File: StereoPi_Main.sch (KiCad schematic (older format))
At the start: 39 parts

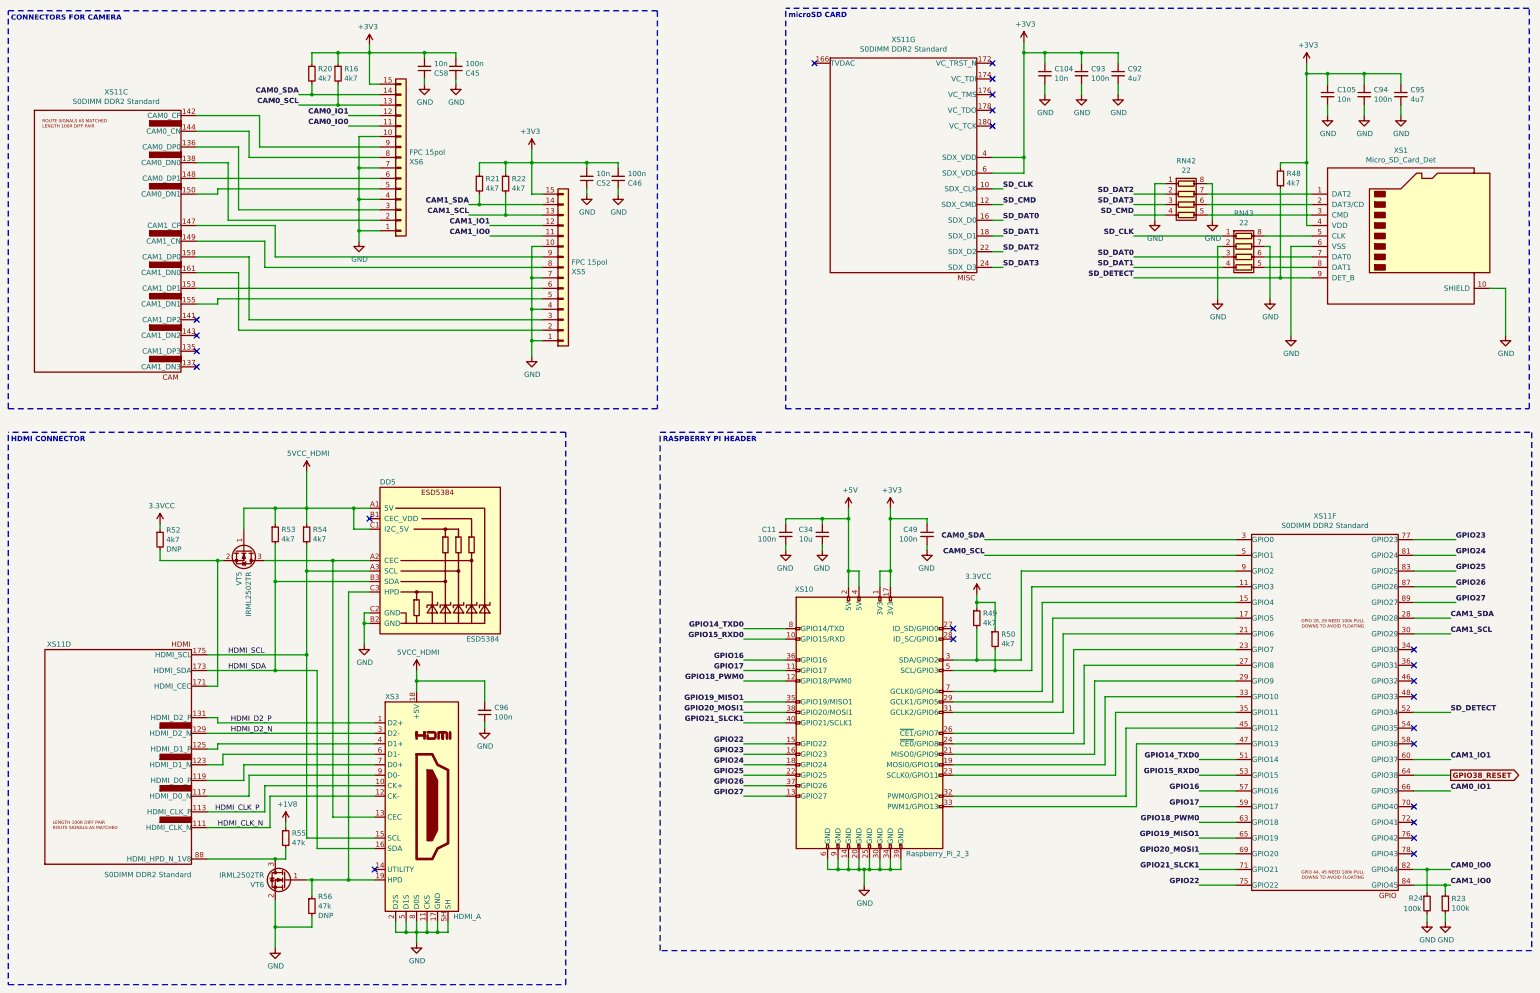
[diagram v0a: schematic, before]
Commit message: added Voltages to Caps, reformatted labels
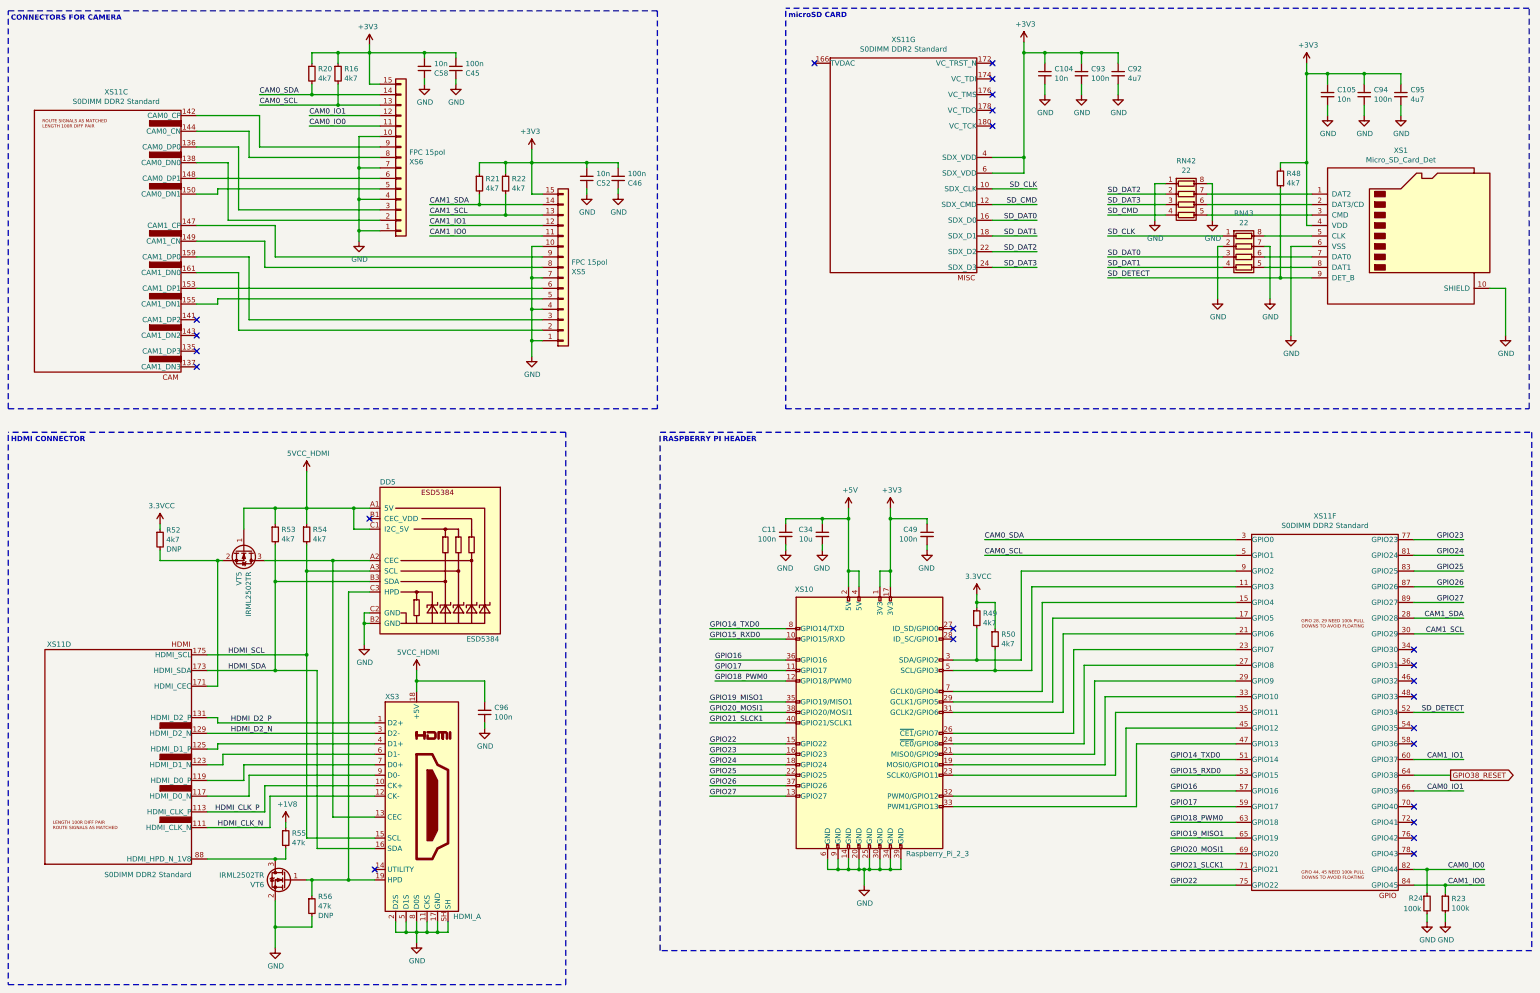
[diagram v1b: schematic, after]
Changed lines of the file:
@@
 EESchema Schematic File Version 4
 LIBS:StereoPi-cache
-EELAYER 26 0
+EELAYER 30 0
 EELAYER END
 $Descr A3 16535 11693
@@
 Wire Wire Line
 	2850 2300 4600 2300
-Text Label 14825 8900 0    50   ~ 10
+Text Label 15150 8900 2    50   ~ 0
 CAM0_IO0
 Wire Wire Line
-	14825 8900 14600 8900
-Text Label 14825 8150 0    50   ~ 10
+	15150 8900 14600 8900
+Text Label 14950 8150 2    50   ~ 0
 CAM0_IO1
-Text Label 10375 5900 2    50   ~ 10
+Text Label 10375 5900 0    50   ~ 0
 CAM0_SCL
-Text Label 10375 5750 2    50   ~ 10
+Text Label 10375 5750 0    50   ~ 0
 CAM0_SDA
 Wire Wire Line
-	14825 8150 14475 8150
-Text Label 3825 1500 2    50   ~ 10
+	14950 8150 14475 8150
+Text Label 3450 1500 0    50   ~ 0
 CAM0_SDA
-Text Label 3825 1600 2    50   ~ 10
+Text Label 3450 1600 0    50   ~ 0
 CAM0_SCL
-Text Label 4300 1800 2    50   ~ 10
+Text Label 3925 1800 0    50   ~ 0
 CAM0_IO0
-Text Label 4300 1700 2    50   ~ 10
+Text Label 3925 1700 0    50   ~ 0
 CAM0_IO1
 Wire Wire Line
-	4600 1700 4300 1700
-Wire Wire Line
-	4600 1800 4300 1800
+	4600 1700 3925 1700
+Wire Wire Line
+	4600 1800 3925 1800
 $Comp
 L power:GND #PWR0108
@@
 Wire Wire Line
 	4400 2200 4400 2500
-Text Label 14825 9050 0    50   ~ 10
+Text Label 15150 9050 2    50   ~ 0
 CAM1_IO0
 Wire Wire Line
-	14825 9050 14775 9050
-Text Label 5650 2850 2    50   ~ 10
+	15150 9050 14775 9050
+Text Label 5075 2850 0    50   ~ 0
 CAM1_IO0
-Text Label 14825 7850 0    50   ~ 10
+Text Label 14950 7850 2    50   ~ 0
 CAM1_IO1
 Wire Wire Line
-	14825 7850 14475 7850
-Text Label 5650 2750 2    50   ~ 10
+	14950 7850 14475 7850
+Text Label 5075 2750 0    50   ~ 0
 CAM1_IO1
-Text Label 14825 6650 0    50   ~ 10
+Text Label 14950 6650 2    50   ~ 0
 CAM1_SCL
-Text Label 14825 6500 0    50   ~ 10
+Text Label 14950 6500 2    50   ~ 0
 CAM1_SDA
-Text Label 5450 2650 2    50   ~ 10
+Text Label 5075 2650 0    50   ~ 0
 CAM1_SCL
-Text Label 5450 2550 2    50   ~ 10
+Text Label 5075 2550 0    50   ~ 0
 CAM1_SDA
 Wire Wire Line
-	14825 6500 14475 6500
-Wire Wire Line
-	14825 6650 14475 6650
-Wire Wire Line
-	5450 2550 5550 2550
-Wire Wire Line
-	5450 2650 5800 2650
-Wire Wire Line
-	5650 2750 6150 2750
-Wire Wire Line
-	5650 2850 6150 2850
+	14950 6500 14475 6500
+Wire Wire Line
+	14950 6650 14475 6650
+Wire Wire Line
+	5075 2550 5550 2550
+Wire Wire Line
+	5075 2650 5800 2650
+Wire Wire Line
+	5075 2750 6150 2750
+Wire Wire Line
+	5075 2850 6150 2850
 $Comp
 L Connector:Raspberry_Pi_2_3 XS10
@@
 	1    0    0    -1
 $EndComp
-Text Label 14825 7400 0    50   ~ 10
+Text Label 14950 7400 2    50   ~ 0
 SD_DETECT
 Wire Wire Line
-	14475 7400 14825 7400
-Text Label 11800 3250 2    50   ~ 10
+	14475 7400 14950 7400
+Text Label 11550 3250 0    50   ~ 0
 SD_DETECT
 Wire Wire Line
-	11800 3250 13200 3250
+	11550 3250 13200 3250
 $Comp
 L Device:R_Small R48
@@
 NoConn ~ 10450 1800
 NoConn ~ 8750 1200
-Text Label 11800 2450 2    50   ~ 10
+Text Label 11550 2450 0    50   ~ 0
 SD_DAT2
-Text Label 11800 2550 2    50   ~ 10
+Text Label 11550 2550 0    50   ~ 0
 SD_DAT3
-Text Label 11800 3050 2    50   ~ 10
+Text Label 11550 3050 0    50   ~ 0
 SD_DAT0
-Text Label 11800 3150 2    50   ~ 10
+Text Label 11550 3150 0    50   ~ 0
 SD_DAT1
-Text Label 10550 3000 0    50   ~ 10
+Text Label 10875 3000 2    50   ~ 0
 SD_DAT2
-Text Label 10550 3150 0    50   ~ 10
+Text Label 10875 3150 2    50   ~ 0
 SD_DAT3
-Text Label 10550 2700 0    50   ~ 10
+Text Label 10875 2700 2    50   ~ 0
 SD_DAT0
-Text Label 10550 2850 0    50   ~ 10
+Text Label 10875 2850 2    50   ~ 0
 SD_DAT1
 Wire Wire Line
-	10550 2700 10450 2700
-Wire Wire Line
-	10550 2850 10450 2850
-Wire Wire Line
-	10550 3000 10450 3000
-Wire Wire Line
-	10550 3150 10450 3150
-Text Label 11800 2650 2    50   ~ 10
+	10875 2700 10450 2700
+Wire Wire Line
+	10875 2850 10450 2850
+Wire Wire Line
+	10875 3000 10450 3000
+Wire Wire Line
+	10875 3150 10450 3150
+Text Label 11550 2650 0    50   ~ 0
 SD_CMD
-Text Label 11800 2850 2    50   ~ 10
+Text Label 11550 2850 0    50   ~ 0
 SD_CLK
 Wire Wire Line
 	13500 2850 13050 2850
-Text Label 10550 2400 0    50   ~ 10
+Text Label 10875 2400 2    50   ~ 0
 SD_CLK
-Text Label 10550 2550 0    50   ~ 10
+Text Label 10875 2550 2    50   ~ 0
 SD_CMD
 Wire Wire Line
-	10550 2400 10450 2400
-Wire Wire Line
-	10550 2550 10450 2550
+	10875 2400 10450 2400
+Wire Wire Line
+	10875 2550 10450 2550
 $Comp
 L Device:R_Pack04 RN42
@@
 	13500 2650 12500 2650
 Wire Wire Line
-	12100 2450 11800 2450
-Wire Wire Line
-	12100 2550 11800 2550
-Wire Wire Line
-	12100 2650 11800 2650
+	12100 2450 11550 2450
+Wire Wire Line
+	12100 2550 11550 2550
+Wire Wire Line
+	12100 2650 11550 2650
 $Comp
 L Device:R_Pack04 RN43
@@
 	13500 3150 13050 3150
 Wire Wire Line
-	12650 2850 11800 2850
-Wire Wire Line
-	12650 3050 11800 3050
-Wire Wire Line
-	12650 3150 11800 3150
+	12650 2850 11550 2850
+Wire Wire Line
+	12650 3050 11550 3050
+Wire Wire Line
+	12650 3150 11550 3150
 $Comp
 L power:GND #PWR0126
@@
 Wire Wire Line
 	11825 7700 12775 7700
-Text Label 12425 7850 2    50   ~ 10
+Text Label 12150 7850 0    50   ~ 0
 GPIO14_TXD0
-Text Label 12425 8000 2    50   ~ 10
+Text Label 12150 8000 0    50   ~ 0
 GPIO15_RXD0
-Text Label 12425 8150 2    50   ~ 10
+Text Label 12150 8150 0    50   ~ 0
 GPIO16
-Text Label 12425 8300 2    50   ~ 10
+Text Label 12150 8300 0    50   ~ 0
 GPIO17
-Text Label 12425 8450 2    50   ~ 10
+Text Label 12150 8450 0    50   ~ 0
 GPIO18_PWM0
-Text Label 12425 8600 2    50   ~ 10
+Text Label 12150 8600 0    50   ~ 0
 GPIO19_MISO1
-Text Label 12425 8750 2    50   ~ 10
+Text Label 12150 8750 0    50   ~ 0
 GPIO20_MOSI1
-Text Label 12425 8900 2    50   ~ 10
+Text Label 12150 8900 0    50   ~ 0
 GPIO21_SLCK1
-Text Label 12425 9050 2    50   ~ 10
+Text Label 12150 9050 0    50   ~ 0
 GPIO22
-Text Label 8075 6600 2    50   ~ 10
+Text Label 7750 6600 0    50   ~ 0
 GPIO14_TXD0
-Text Label 8075 6700 2    50   ~ 10
+Text Label 7750 6700 0    50   ~ 0
 GPIO15_RXD0
-Text Label 8075 6900 2    50   ~ 10
+Text Label 7800 6900 0    50   ~ 0
 GPIO16
-Text Label 8075 7000 2    50   ~ 10
+Text Label 7800 7000 0    50   ~ 0
 GPIO17
-Text Label 8075 7100 2    50   ~ 10
+Text Label 7800 7100 0    50   ~ 0
 GPIO18_PWM0
-Text Label 8075 7300 2    50   ~ 10
+Text Label 7750 7300 0    50   ~ 0
 GPIO19_MISO1
-Text Label 8075 7400 2    50   ~ 10
+Text Label 7750 7400 0    50   ~ 0
 GPIO20_MOSI1
-Text Label 8075 7500 2    50   ~ 10
+Text Label 7750 7500 0    50   ~ 0
 GPIO21_SLCK1
-Text Label 8075 7700 2    50   ~ 10
+Text Label 7750 7700 0    50   ~ 0
 GPIO22
-Text Label 14875 5750 0    50   ~ 10
+Text Label 14950 5750 2    50   ~ 0
 GPIO23
-Text Label 14875 5900 0    50   ~ 10
+Text Label 14950 5900 2    50   ~ 0
 GPIO24
-Text Label 14875 6050 0    50   ~ 10
+Text Label 14950 6050 2    50   ~ 0
 GPIO25
-Text Label 14875 6200 0    50   ~ 10
+Text Label 14950 6200 2    50   ~ 0
 GPIO26
-Text Label 14875 6350 0    50   ~ 10
+Text Label 14950 6350 2    50   ~ 0
 GPIO27
 Wire Wire Line
-	14875 6350 14475 6350
-Wire Wire Line
-	14875 6200 14475 6200
-Wire Wire Line
-	14875 6050 14475 6050
-Wire Wire Line
-	14875 5900 14475 5900
-Wire Wire Line
-	14875 5750 14475 5750
-Text Label 8075 7800 2    50   ~ 10
+	14950 6350 14475 6350
+Wire Wire Line
+	14950 6200 14475 6200
+Wire Wire Line
+	14950 6050 14475 6050
+Wire Wire Line
+	14950 5900 14475 5900
+Wire Wire Line
+	14950 5750 14475 5750
+Text Label 7750 7800 0    50   ~ 0
 GPIO23
-Text Label 8075 7900 2    50   ~ 10
+Text Label 7750 7900 0    50   ~ 0
 GPIO24
-Text Label 8075 8000 2    50   ~ 10
+Text Label 7750 8000 0    50   ~ 0
 GPIO25
-Text Label 8075 8100 2    50   ~ 10
+Text Label 7750 8100 0    50   ~ 0
 GPIO26
-Text Label 8075 8200 2    50   ~ 10
+Text Label 7750 8200 0    50   ~ 0
 GPIO27
 Wire Wire Line
-	8075 7700 8475 7700
-Wire Wire Line
-	8075 7800 8475 7800
-Wire Wire Line
-	8075 7900 8475 7900
-Wire Wire Line
-	8075 8000 8475 8000
-Wire Wire Line
-	8075 8100 8475 8100
-Wire Wire Line
-	8075 8200 8475 8200
-Wire Wire Line
-	8075 7300 8475 7300
-Wire Wire Line
-	8075 7400 8475 7400
-Wire Wire Line
-	8075 7500 8475 7500
-Wire Wire Line
-	8075 7100 8475 7100
-Wire Wire Line
-	8075 7000 8475 7000
-Wire Wire Line
-	8075 6900 8475 6900
-Wire Wire Line
-	8075 6600 8475 6600
-Wire Wire Line
-	8075 6700 8475 6700
-Wire Wire Line
-	12425 7850 12775 7850
-Wire Wire Line
-	12425 8000 12775 8000
-Wire Wire Line
-	12425 8150 12775 8150
-Wire Wire Line
-	12775 8300 12425 8300
-Wire Wire Line
-	12425 8450 12775 8450
-Wire Wire Line
-	12775 8600 12425 8600
-Wire Wire Line
-	12425 8750 12775 8750
-Wire Wire Line
-	12775 8900 12425 8900
-Wire Wire Line
-	12425 9050 12775 9050
+	7750 7700 8475 7700
+Wire Wire Line
+	7750 7800 8475 7800
+Wire Wire Line
+	7750 7900 8475 7900
+Wire Wire Line
+	7750 8000 8475 8000
+Wire Wire Line
+	7750 8100 8475 8100
+Wire Wire Line
+	7750 8200 8475 8200
+Wire Wire Line
+	7750 7300 8475 7300
+Wire Wire Line
+	7750 7400 8475 7400
+Wire Wire Line
+	7750 7500 8475 7500
+Wire Wire Line
+	7800 7100 8475 7100
+Wire Wire Line
+	7800 7000 8475 7000
+Wire Wire Line
+	7800 6900 8475 6900
+Wire Wire Line
+	7750 6600 8475 6600
+Wire Wire Line
+	7750 6700 8475 6700
+Wire Wire Line
+	12150 7850 12775 7850
+Wire Wire Line
+	12150 8000 12775 8000
+Wire Wire Line
+	12150 8150 12775 8150
+Wire Wire Line
+	12775 8300 12150 8300
+Wire Wire Line
+	12150 8450 12775 8450
+Wire Wire Line
+	12775 8600 12150 8600
+Wire Wire Line
+	12150 8750 12775 8750
+Wire Wire Line
+	12775 8900 12150 8900
+Wire Wire Line
+	12150 9050 12775 9050
 $Comp
 L power:GND #PWR0131
@@
 	3950 1400 3950 1500
 Wire Wire Line
-	3825 1500 3950 1500
+	3450 1500 3950 1500
 Connection ~ 3950 1500
 Wire Wire Line
@@
 	4200 1400 4200 1600
 Wire Wire Line
-	3825 1600 4200 1600
+	3450 1600 4200 1600
 Connection ~ 4200 1600
 Wire Wire Line
@@
 Wire Wire Line
 	6050 2150 6050 2025
-Text GLabel 14825 8000 2    50   Output ~ 10
+Text GLabel 14825 8000 2    50   Output ~ 0
 GPIO38_RESET
 Wire Wire Line
